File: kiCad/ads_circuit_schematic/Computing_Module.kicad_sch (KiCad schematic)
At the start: 0 parts

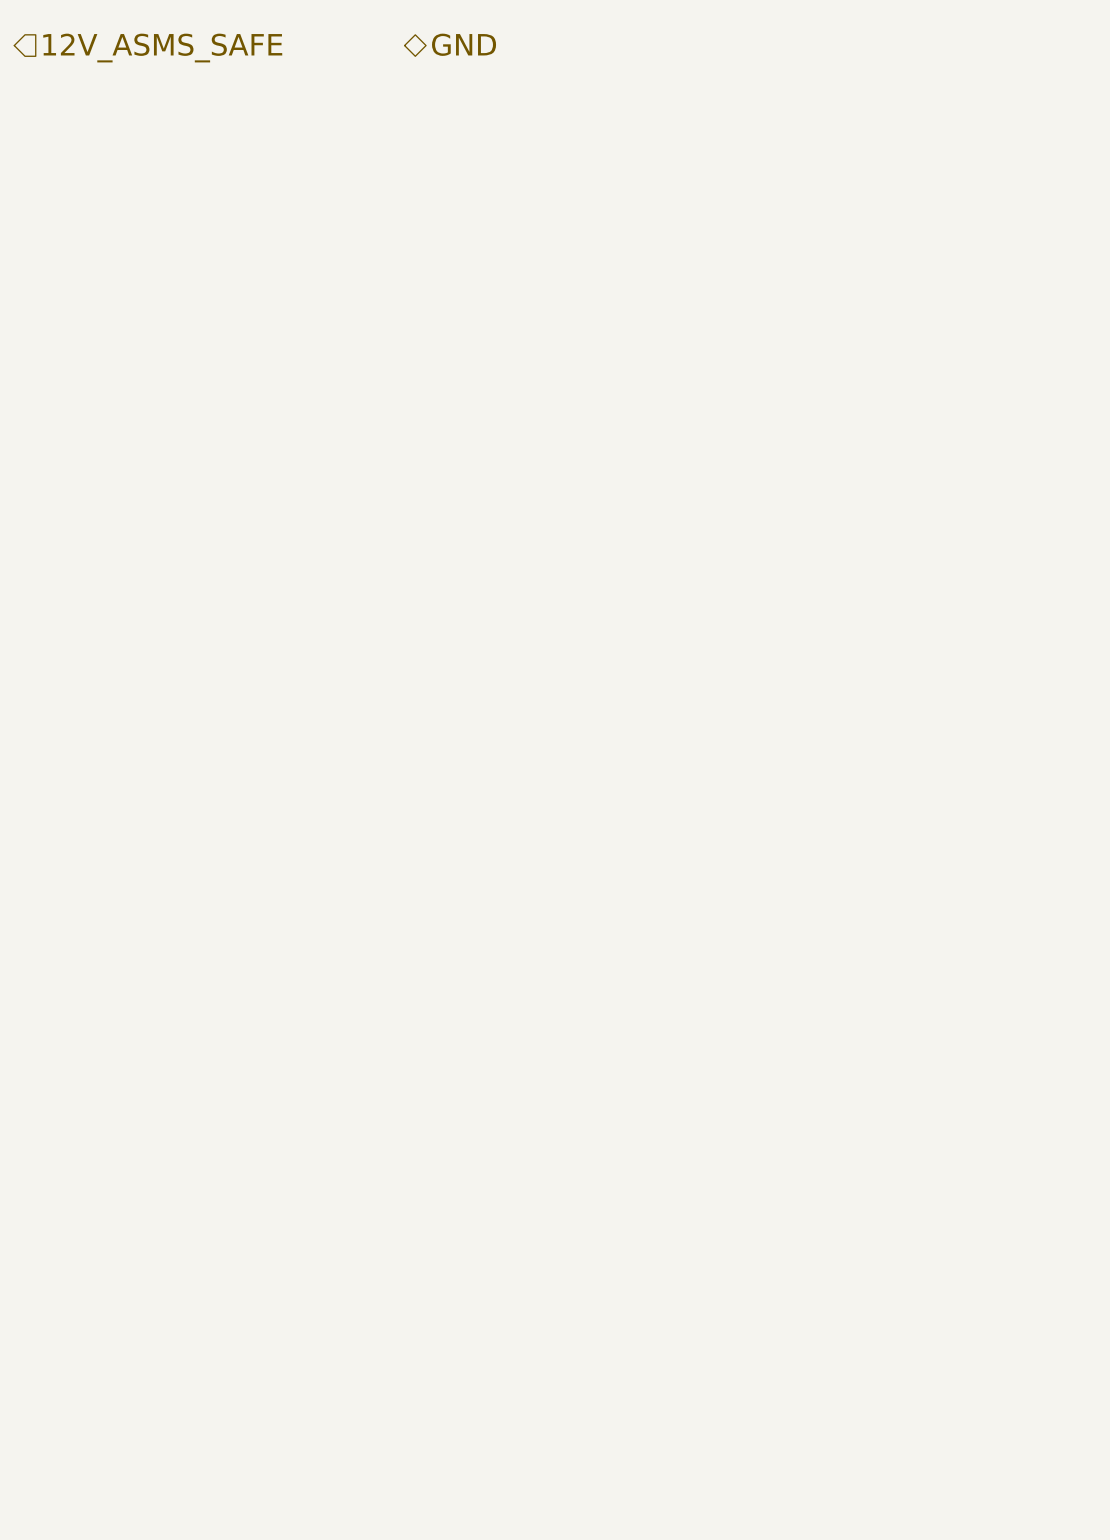
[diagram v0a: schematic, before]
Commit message: Added new symbols for linear actuators, added fuses, added 5V step down
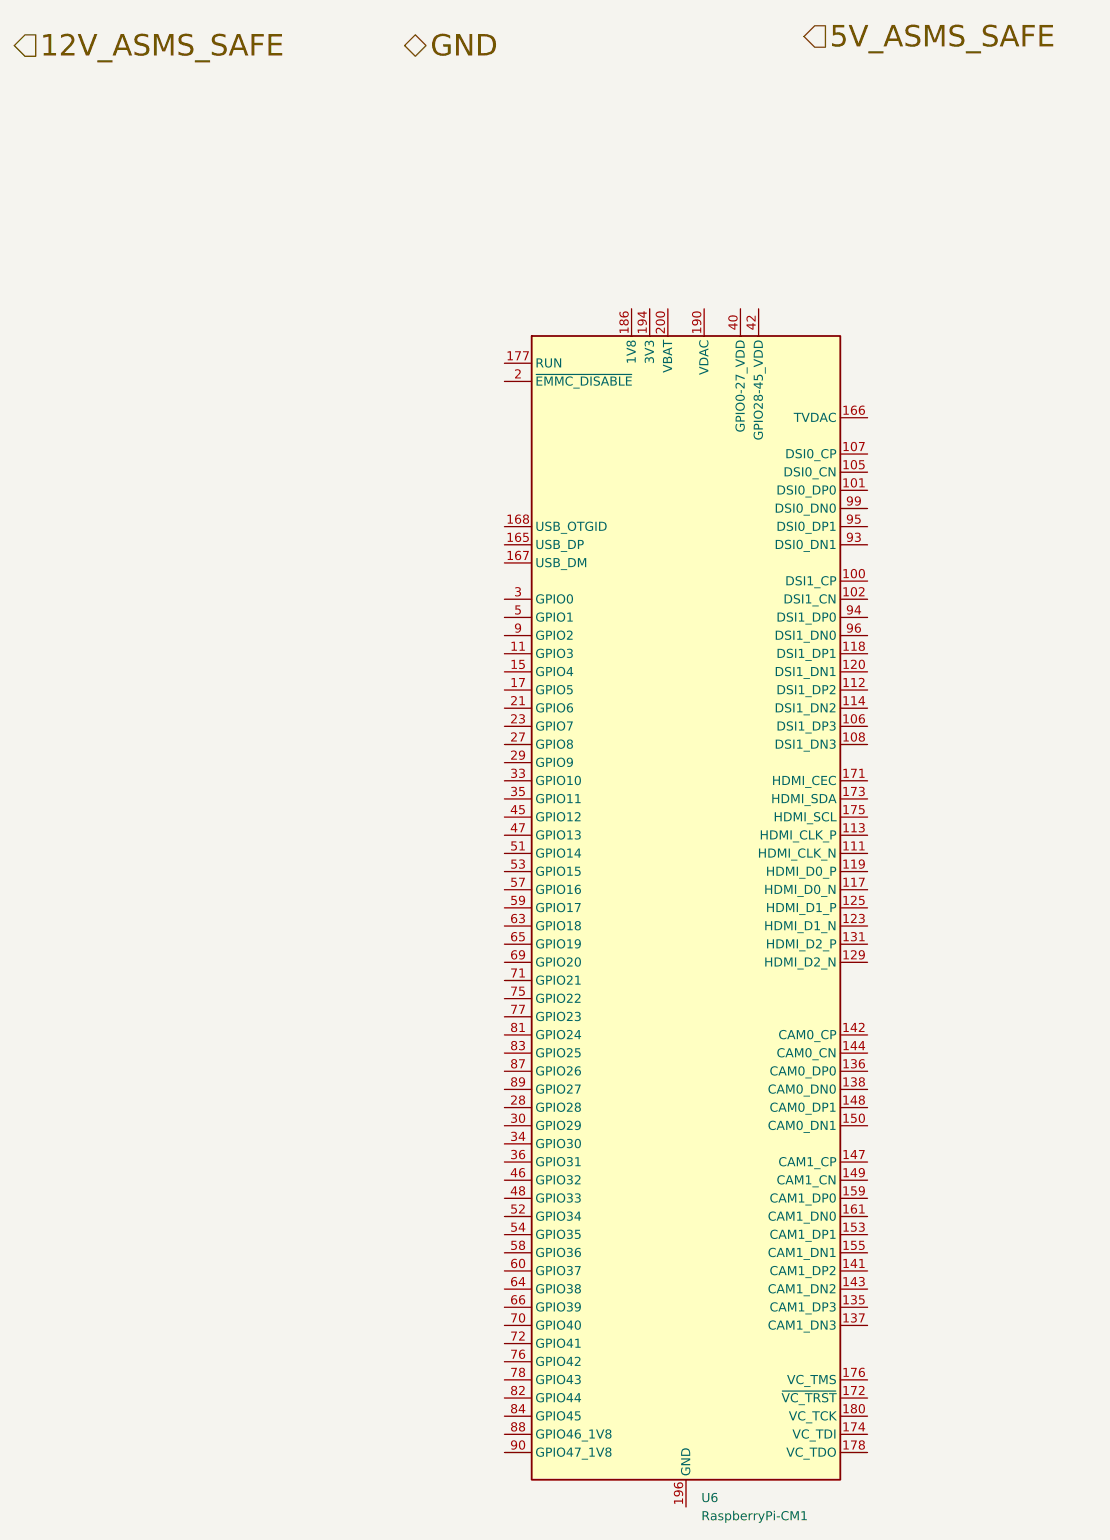
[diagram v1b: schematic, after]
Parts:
- added U6: RaspberryPi-CM1, symbol MCU_Module:RaspberryPi-CM1
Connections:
- new net: U6.1 (GND), U6.103 (GND), U6.104 (GND), U6.109 (GND), U6.110 (GND), U6.115 (GND), U6.116 (GND), U6.121 (GND), U6.122 (GND), U6.127 (GND), U6.13 (GND), U6.133 (GND), U6.134 (GND), U6.139 (GND), U6.140 (GND), U6.145 (GND), U6.146 (GND), U6.151 (GND), U6.152 (GND), U6.157 (GND), U6.163 (GND), U6.164 (GND), U6.169 (GND), U6.170 (GND), U6.181 (GND), U6.182 (GND), U6.187 (GND), U6.188 (GND), U6.19 (GND), U6.195 (GND), U6.196 (GND), U6.25 (GND), U6.26 (GND), U6.31 (GND), U6.32 (GND), U6.37 (GND), U6.38 (GND), U6.43 (GND), U6.44 (GND), U6.49 (GND), U6.50 (GND), U6.55 (GND), U6.56 (GND), U6.61 (GND), U6.62 (GND), U6.67 (GND), U6.68 (GND), U6.7 (GND), U6.73 (GND), U6.74 (GND), U6.79 (GND), U6.80 (GND), U6.85 (GND), U6.86 (GND), U6.91 (GND), U6.92 (GND), U6.97 (GND), U6.98 (GND)
- new net: U6.183 (1V8), U6.184 (1V8), U6.185 (1V8), U6.186 (1V8)
- new net: U6.189 (VDAC), U6.190 (VDAC)
- new net: U6.191 (3V3), U6.192 (3V3), U6.193 (3V3), U6.194 (3V3)
- new net: U6.197 (VBAT), U6.198 (VBAT), U6.199 (VBAT), U6.200 (VBAT)
- new net: U6.39 (GPIO0-27_VDD), U6.40 (GPIO0-27_VDD)
- new net: U6.41 (GPIO28-45_VDD), U6.42 (GPIO28-45_VDD)
